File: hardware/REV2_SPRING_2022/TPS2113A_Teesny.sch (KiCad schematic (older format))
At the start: 7 parts, among them U201 TPS2113ADRBR

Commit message: wip switch wire terminals
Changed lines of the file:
@@
 $Descr A4 11693 8268
 encoding utf-8
-Sheet 3 3
+Sheet 2 3
 Title ""
 Date ""
@@
 AR Path="/61A02CEE/61AB462E" Ref="U201"  Part="1"
 AR Path="/619AC3BC/61AB462E" Ref="U301"  Part="1"
-F 0 "U301" H 6600 3720 50  0000 C CNN
+F 0 "U201" H 6600 3720 50  0000 C CNN
 F 1 "TPS2113ADRBR" H 6600 3629 50  0000 C CNN
 F 2 "Package_SO:TSSOP-8_4.4x3mm_P0.65mm" H 6600 3050 50  0001 L BNN
@@
 AR Path="/619AC3BC/61AB4644" Ref="C301"  Part="1"
 AR Path="/61A02CEE/61AB4644" Ref="C201"  Part="1"
-F 0 "C301" H 4115 3346 50  0000 L CNN
+F 0 "C201" H 4115 3346 50  0000 L CNN
 F 1 "C_0.1u" H 4115 3255 50  0000 L CNN
 F 2 "Capacitor_SMD:C_0805_2012Metric_Pad1.18x1.45mm_HandSolder" H 4038 3150 50  0001 C CNN
@@
 AR Path="/619AC3BC/61AB464C" Ref="C302"  Part="1"
 AR Path="/61A02CEE/61AB464C" Ref="C202"  Part="1"
-F 0 "C302" H 5515 3346 50  0000 L CNN
+F 0 "C202" H 5515 3346 50  0000 L CNN
 F 1 "C_0.1u" H 5000 3300 50  0000 L CNN
 F 2 "Capacitor_SMD:C_0805_2012Metric_Pad1.18x1.45mm_HandSolder" H 5438 3150 50  0001 C CNN
@@
 AR Path="/619AC3BC/61AB465E" Ref="R301"  Part="1"
 AR Path="/61A02CEE/61AB465E" Ref="R201"  Part="1"
-F 0 "R301" H 5620 2496 50  0000 L CNN
+F 0 "R201" H 5620 2496 50  0000 L CNN
 F 1 "R_200" H 5620 2405 50  0000 L CNN
 F 2 "Resistor_SMD:R_0805_2012Metric_Pad1.20x1.40mm_HandSolder" V 5480 2450 50  0001 C CNN
@@
 AR Path="/619AC3BC/61AB46B4" Ref="R302"  Part="1"
 AR Path="/61A02CEE/61AB46B4" Ref="R202"  Part="1"
-F 0 "R302" H 7820 2996 50  0000 L CNN
+F 0 "R202" H 7820 2996 50  0000 L CNN
 F 1 "R_10k" H 7820 2905 50  0000 L CNN
 F 2 "Resistor_SMD:R_0805_2012Metric_Pad1.20x1.40mm_HandSolder" V 7680 2950 50  0001 C CNN
@@
 AR Path="/619AC3BC/61AB46C3" Ref="C303"  Part="1"
 AR Path="/61A02CEE/61AB46C3" Ref="C203"  Part="1"
-F 0 "C303" H 8415 1996 50  0000 L CNN
+F 0 "C203" H 8415 1996 50  0000 L CNN
 F 1 "C_0.1u" H 8415 1905 50  0000 L CNN
 F 2 "Capacitor_SMD:C_0805_2012Metric_Pad1.18x1.45mm_HandSolder" H 8338 1800 50  0001 C CNN
@@
 AR Path="/619AC3BC/619F982E" Ref="R303"  Part="1"
 AR Path="/61A02CEE/619F982E" Ref="R203"  Part="1"
-F 0 "R303" H 5620 1946 50  0000 L CNN
+F 0 "R203" H 5620 1946 50  0000 L CNN
 F 1 "R_200" H 5620 1855 50  0000 L CNN
 F 2 "Resistor_SMD:R_0805_2012Metric_Pad1.20x1.40mm_HandSolder" V 5480 1900 50  0001 C CNN

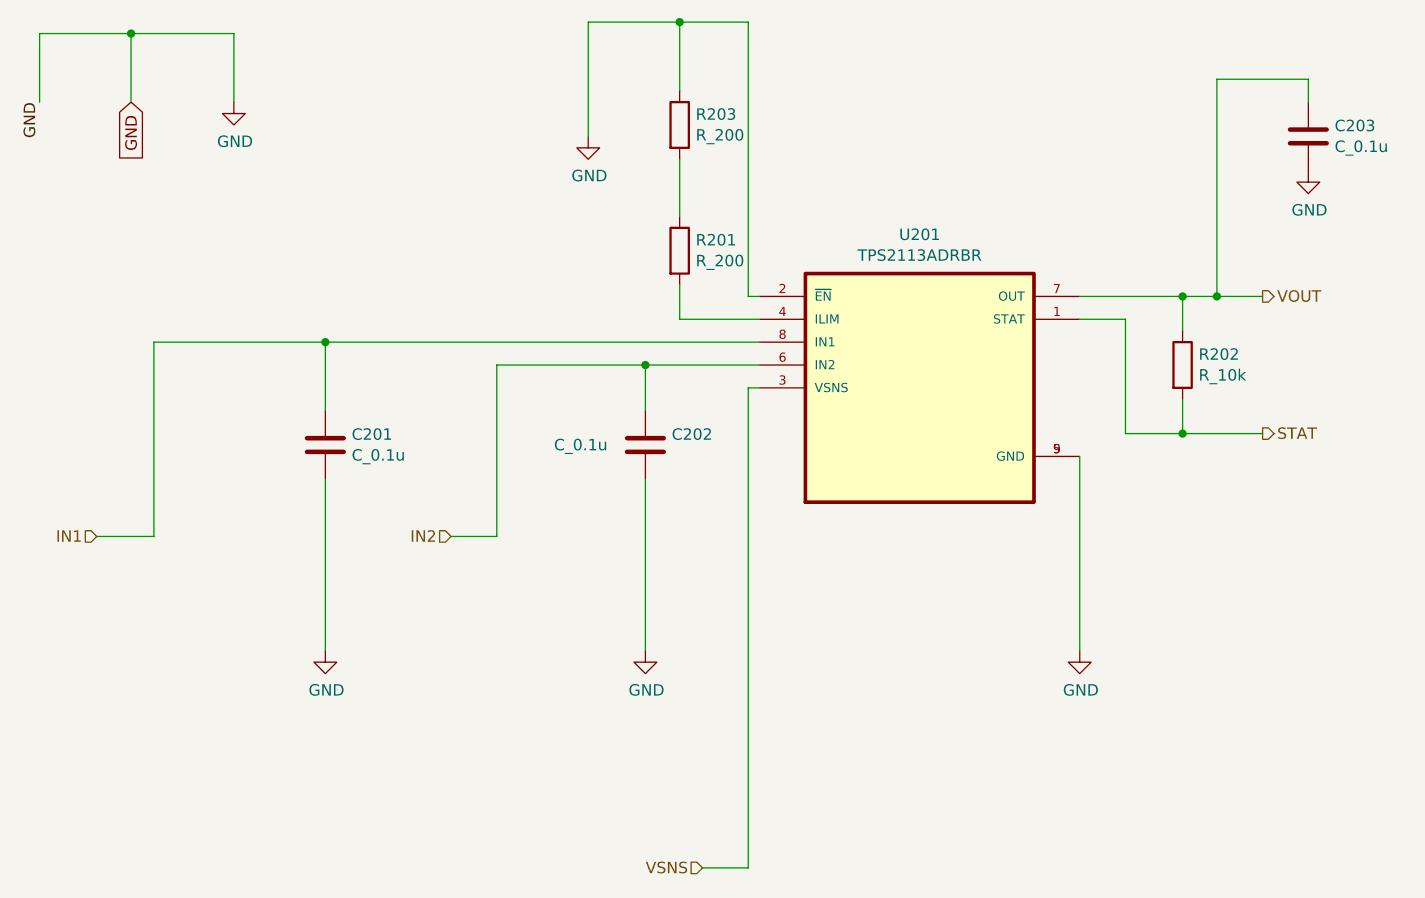
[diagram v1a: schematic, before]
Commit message: add pullup resistors on TPS stat pins
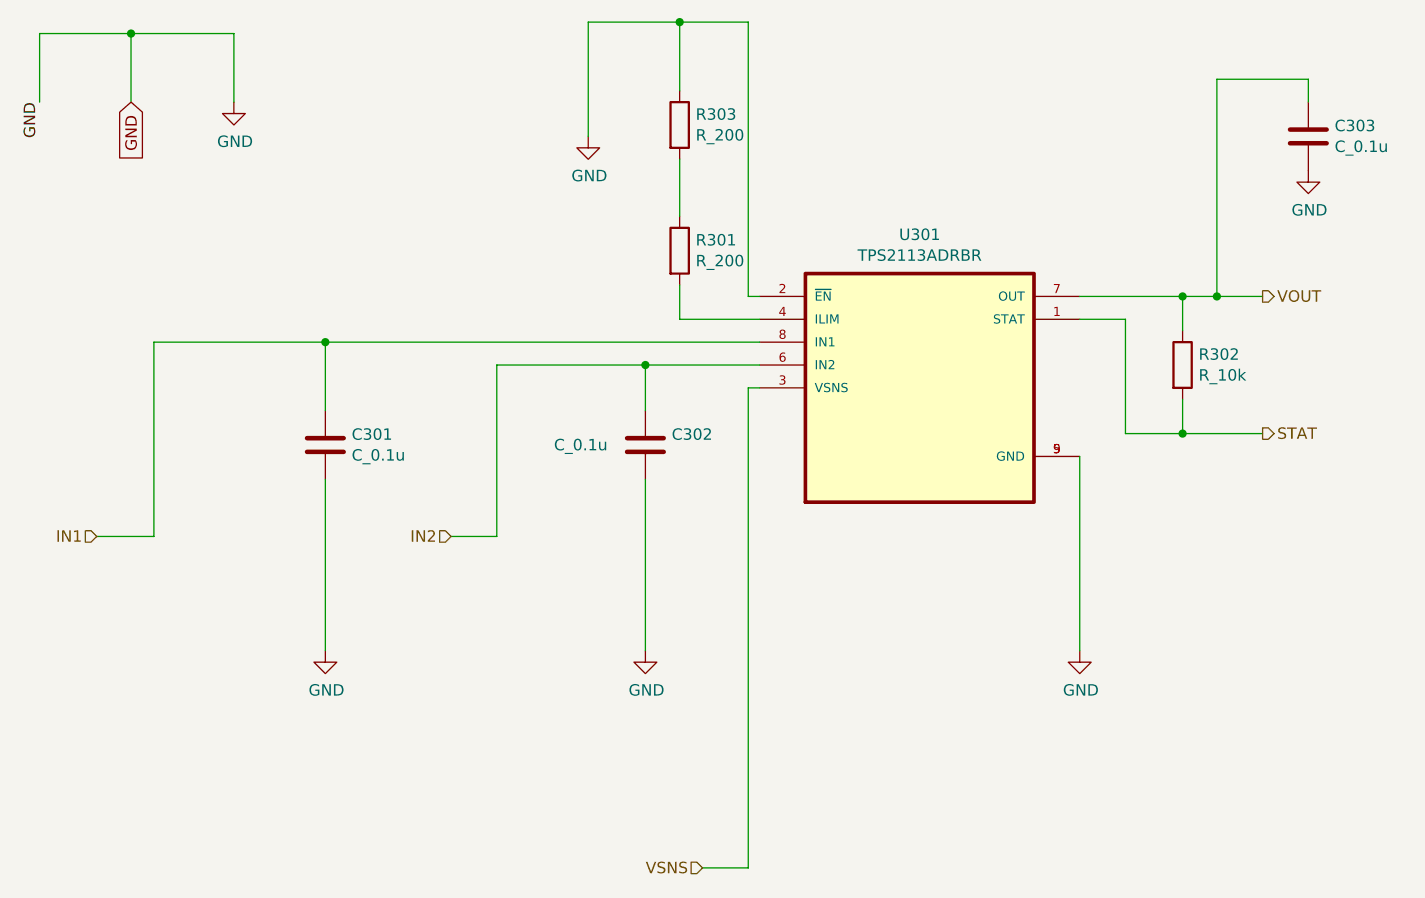
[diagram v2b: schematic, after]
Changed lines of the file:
@@
 AR Path="/61A02CEE/61AB462E" Ref="U201"  Part="1"
 AR Path="/619AC3BC/61AB462E" Ref="U301"  Part="1"
-F 0 "U201" H 6600 3720 50  0000 C CNN
+F 0 "U301" H 6600 3720 50  0000 C CNN
 F 1 "TPS2113ADRBR" H 6600 3629 50  0000 C CNN
 F 2 "Package_SO:TSSOP-8_4.4x3mm_P0.65mm" H 6600 3050 50  0001 L BNN
@@
 AR Path="/619AC3BC/61AB4644" Ref="C301"  Part="1"
 AR Path="/61A02CEE/61AB4644" Ref="C201"  Part="1"
-F 0 "C201" H 4115 3346 50  0000 L CNN
+F 0 "C301" H 4115 3346 50  0000 L CNN
 F 1 "C_0.1u" H 4115 3255 50  0000 L CNN
 F 2 "Capacitor_SMD:C_0805_2012Metric_Pad1.18x1.45mm_HandSolder" H 4038 3150 50  0001 C CNN
@@
 AR Path="/619AC3BC/61AB464C" Ref="C302"  Part="1"
 AR Path="/61A02CEE/61AB464C" Ref="C202"  Part="1"
-F 0 "C202" H 5515 3346 50  0000 L CNN
+F 0 "C302" H 5515 3346 50  0000 L CNN
 F 1 "C_0.1u" H 5000 3300 50  0000 L CNN
 F 2 "Capacitor_SMD:C_0805_2012Metric_Pad1.18x1.45mm_HandSolder" H 5438 3150 50  0001 C CNN
@@
 AR Path="/619AC3BC/61AB465E" Ref="R301"  Part="1"
 AR Path="/61A02CEE/61AB465E" Ref="R201"  Part="1"
-F 0 "R201" H 5620 2496 50  0000 L CNN
+F 0 "R301" H 5620 2496 50  0000 L CNN
 F 1 "R_200" H 5620 2405 50  0000 L CNN
 F 2 "Resistor_SMD:R_0805_2012Metric_Pad1.20x1.40mm_HandSolder" V 5480 2450 50  0001 C CNN
@@
 AR Path="/619AC3BC/61AB46B4" Ref="R302"  Part="1"
 AR Path="/61A02CEE/61AB46B4" Ref="R202"  Part="1"
-F 0 "R202" H 7820 2996 50  0000 L CNN
+F 0 "R302" H 7820 2996 50  0000 L CNN
 F 1 "R_10k" H 7820 2905 50  0000 L CNN
 F 2 "Resistor_SMD:R_0805_2012Metric_Pad1.20x1.40mm_HandSolder" V 7680 2950 50  0001 C CNN
@@
 AR Path="/619AC3BC/61AB46C3" Ref="C303"  Part="1"
 AR Path="/61A02CEE/61AB46C3" Ref="C203"  Part="1"
-F 0 "C203" H 8415 1996 50  0000 L CNN
+F 0 "C303" H 8415 1996 50  0000 L CNN
 F 1 "C_0.1u" H 8415 1905 50  0000 L CNN
 F 2 "Capacitor_SMD:C_0805_2012Metric_Pad1.18x1.45mm_HandSolder" H 8338 1800 50  0001 C CNN
@@
 AR Path="/619AC3BC/619F982E" Ref="R303"  Part="1"
 AR Path="/61A02CEE/619F982E" Ref="R203"  Part="1"
-F 0 "R203" H 5620 1946 50  0000 L CNN
+F 0 "R303" H 5620 1946 50  0000 L CNN
 F 1 "R_200" H 5620 1855 50  0000 L CNN
 F 2 "Resistor_SMD:R_0805_2012Metric_Pad1.20x1.40mm_HandSolder" V 5480 1900 50  0001 C CNN
